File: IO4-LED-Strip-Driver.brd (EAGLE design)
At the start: 109.9 x 100 mm, 21 parts, among them Q1 DMN4468, Q2 DMN4468, Q3 DMN4468, Q7 DMN4468

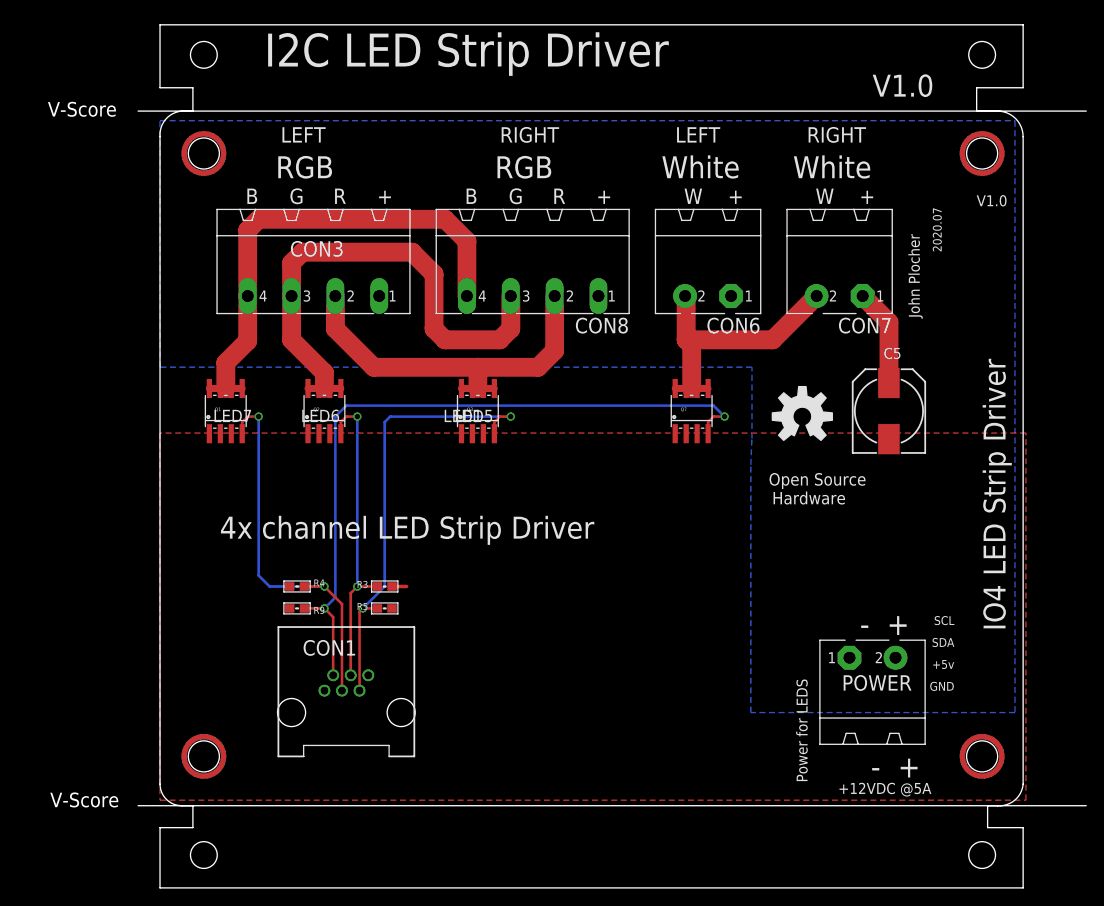
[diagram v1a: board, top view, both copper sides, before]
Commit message: silkscreen changes
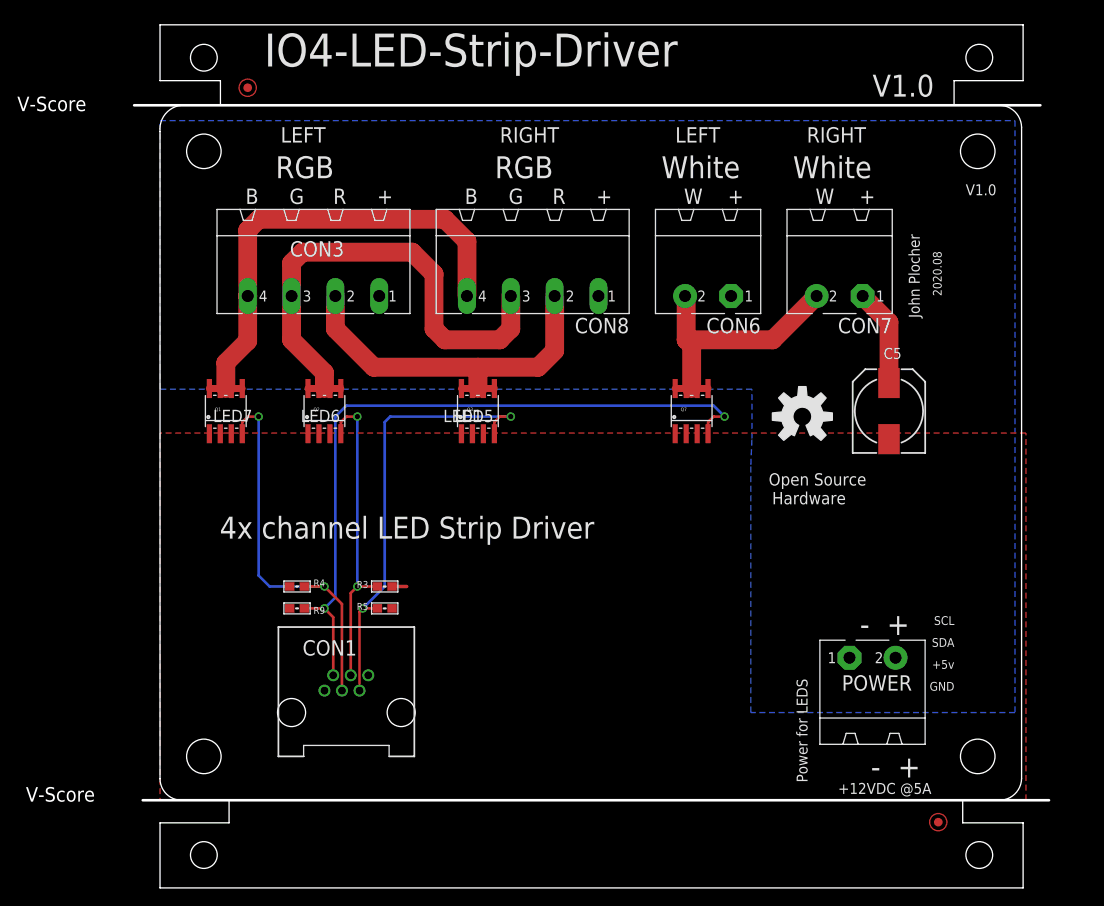
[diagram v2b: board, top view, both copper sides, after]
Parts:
- removed U$1, U$2, U$3, U$4: MOUNTINGHOLE, SPCoast:MOUNTINGHOLE
- added FID1, FID2: FIDUCIAL, SPCoast:FIDUCIAL_1MM
- BOARD1: value BOARD80X100-TEMPLATE -> BOARD80X100; device SPCoast:BOARD-10X8-TEMPLATE -> SPCoast:BOARD-DINRAIL-3.17INX10CM
- C5: value 150uF -> 220uF
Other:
- board size 109.9 x 100 mm -> 106 x 100 mm
- board text added: "2020.08"
- board text added: ">DRAWING_NAME"
- board text removed: "2020.07"
- board text removed: "I2C LED Strip Driver"
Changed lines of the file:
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@@
 <grid distance="50" unitdist="mil" unit="mil" style="dots" multiple="2" display="yes" altdistance="25" altunitdist="mil" altunit="mil"/>
 <layers>
-<layer number="1" name="Top" color="4" fill="1" visible="no" active="yes"/>
-<layer number="16" name="Bottom" color="2" fill="1" visible="no" active="yes"/>
+<layer number="1" name="Top" color="4" fill="1" visible="yes" active="yes"/>
+<layer number="16" name="Bottom" color="2" fill="1" visible="yes" active="yes"/>
 <layer number="17" name="Pads" color="23" fill="1" visible="yes" active="yes"/>
 <layer number="18" name="Vias" color="29" fill="1" visible="yes" active="yes"/>
-<layer number="19" name="Unrouted" color="6" fill="1" visible="no" active="yes"/>
+<layer number="19" name="Unrouted" color="6" fill="1" visible="yes" active="yes"/>
 <layer number="20" name="Dimension" color="15" fill="1" visible="yes" active="yes"/>
 <layer number="21" name="tPlace" color="19" fill="1" visible="yes" active="yes"/>
 <layer number="22" name="bPlace" color="17" fill="1" visible="no" active="yes"/>
-<layer number="23" name="tOrigins" color="30" fill="1" visible="no" active="yes"/>
+<layer number="23" name="tOrigins" color="30" fill="1" visible="yes" active="yes"/>
 <layer number="24" name="bOrigins" color="15" fill="1" visible="no" active="yes"/>
-<layer number="25" name="tNames" color="63" fill="1" visible="no" active="yes"/>
+<layer number="25" name="tNames" color="63" fill="1" visible="yes" active="yes"/>
 <layer number="26" name="bNames" color="34" fill="1" visible="no" active="yes"/>
 <layer number="27" name="tValues" color="56" fill="1" visible="yes" active="yes"/>
@@
 <layer number="42" name="bRestrict" color="3" fill="10" visible="no" active="yes"/>
 <layer number="43" name="vRestrict" color="2" fill="10" visible="no" active="yes"/>
-<layer number="44" name="Drills" color="16" fill="1" visible="no" active="yes"/>
-<layer number="45" name="Holes" color="35" fill="1" visible="no" active="yes"/>
+<layer number="44" name="Drills" color="16" fill="1" visible="yes" active="yes"/>
+<layer number="45" name="Holes" color="35" fill="1" visible="yes" active="yes"/>
 <layer number="46" name="Milling" color="50" fill="1" visible="yes" active="yes"/>
-<layer number="47" name="Measures" color="21" fill="1" visible="no" active="yes"/>
+<layer number="47" name="Measures" color="21" fill="1" visible="yes" active="yes"/>
 <layer number="48" name="Document" color="24" fill="1" visible="yes" active="yes"/>
-<layer number="49" name="Reference" color="48" fill="1" visible="no" active="yes"/>
+<layer number="49" name="Reference" color="48" fill="1" visible="yes" active="yes"/>
 <layer number="50" name="dxf" color="7" fill="1" visible="no" active="yes"/>
 <layer number="51" name="tDocu" color="24" fill="1" visible="yes" active="yes"/>
@@
 <board>
 <plain>
-<text x="12.065" y="95.17" size="3.81" layer="21" font="vector" ratio="13" distance="49" rot="SR0">I2C LED Strip Driver</text>
-<text x="94.615" y="78.98" size="1.27" layer="21" font="vector" ratio="10">V1.0</text>
+<text x="12.065" y="95.17" size="3.81" layer="21" font="vector" ratio="13" distance="49" rot="SR0">&gt;DRAWING_NAME</text>
+<text x="93.345" y="80.25" size="1.27" layer="21" font="vector" ratio="10">V1.0</text>
 <text x="9.033" y="13.1318" size="1.778" layer="52" rot="MR180">Made in the PCR, Coast Division, NMRA</text>
 <text x="91.0418" y="11.7152" size="1.4224" layer="52" font="vector" ratio="15" rot="MR0">www. SP Coast .com</text>
@@
 <wire x1="3.953" y1="27.305" x2="11.573" y2="66.802" width="3.81" layer="52"/>
 <text x="89.37625" y="12.16025" size="1.27" layer="21" font="vector" rot="R180">+12VDC @5A</text>
-<text x="97.959971875" y="29.76735625" size="2.54" layer="21" font="vector" ratio="15" rot="SR90">IO4 LED Strip Driver</text>
+<text x="93.810028125" y="78.18264375" size="2.54" layer="21" font="vector" ratio="15" rot="R270">&gt;DRAWING_NAME</text>
 <wire x1="0" y1="60.96" x2="100.33" y2="46.99" width="2.1844" layer="52"/>
 <wire x1="0" y1="35.56" x2="100.33" y2="21.59" width="2.1844" layer="52"/>
@@
 <text x="92.04200625" y="26.402490625" size="1.016" layer="21" font="vector" ratio="10" rot="R180">+5v</text>
 <text x="92.04200625" y="23.862490625" size="1.016" layer="21" font="vector" ratio="10" rot="R180">GND</text>
-<text x="90.565" y="73.66" size="1.016" layer="21" font="vector" ratio="10" rot="R90">2020.07</text>
+<text x="90.565" y="68.58" size="1.016" layer="21" font="vector" ratio="10" rot="R90">2020.08</text>
 <text x="88.025" y="66.04" size="1.27" layer="21" font="vector" ratio="10" rot="R90">John Plocher</text>
 <text x="75.02525" y="12.22375" size="1.27" layer="21" font="vector" rot="R90">Power for LEDS</text>
@@
 </autorouter>
 <elements>
-<element name="BOARD1" library="SPCoast" package="BOARD-10X8-TEMPLATE" value="BOARD80X100-TEMPLATE" x="0" y="0"/>
+<element name="BOARD1" library="SPCoast" package="BOARD-DINRAIL-3.17INX10CM" value="BOARD80X100" x="0" y="0"/>
 <element name="OSHW1" library="SparkFun" package="OSHW-LOGO-L" value="OSHW-LOGOL" x="74.422" y="54.61"/>
-<element name="C5" library="SPCoast" package="0810-CAP" value="150uF" x="84.455" y="55.245" smashed="yes" rot="R90">
+<element name="C5" library="SPCoast" package="0810-CAP" value="220uF" x="84.455" y="55.245" smashed="yes" rot="R90">
 <attribute name="NAME" x="85.925" y="62.565" size="1.27" layer="25" rot="R180"/>
 <attribute name="VALUE" x="87.63" y="55.88" size="1.27" layer="27" font="vector" rot="R180"/>
@@
 <attribute name="VALUE" x="77.47" y="21.59" size="1.778" layer="27" ratio="10"/>
 </element>
-<element name="U$1" library="SPCoast" package="MOUNTINGHOLE" value="MOUNTINGHOLE" x="5.08" y="15.24"/>
-<element name="U$2" library="SPCoast" package="MOUNTINGHOLE" value="MOUNTINGHOLE" x="95.25" y="15.24"/>
-<element name="U$4" library="SPCoast" package="MOUNTINGHOLE" value="MOUNTINGHOLE" x="95.25" y="85.09"/>
-<element name="U$3" library="SPCoast" package="MOUNTINGHOLE" value="MOUNTINGHOLE" x="5.08" y="85.09"/>
 <element name="R5" library="SPCoast" package="0603-RES" value="10k" x="26.035" y="32.385" smashed="yes" rot="R180">
 <attribute name="NAME" x="24.13" y="33.02" size="0.8128" layer="25" font="vector" rot="R180"/>
@@
 <element name="CON7" library="SPCoast" package="MSTBA2" value="" x="78.74" y="73.66" rot="R180"/>
 <element name="CON8" library="SPCoast" package="MSTBA4" value="" x="43.18" y="73.66" rot="R180"/>
+<element name="FID1" library="SPCoast" package="FIDUCIAL_1MM" value="FIDUCIAL" x="10.16" y="92.71"/>
+<element name="FID2" library="SPCoast" package="FIDUCIAL_1MM" value="FIDUCIAL" x="90.17" y="7.62"/>
 </elements>
 <signals>
@@
 <vertex x="68.453" y="49.022"/>
 <vertex x="68.58" y="52.07"/>
-<vertex x="68.58" y="60.325"/>
-<vertex x="0" y="60.325"/>
+<vertex x="68.58" y="57.785"/>
+<vertex x="0" y="57.785"/>
 <vertex x="0" y="88.9"/>
 <vertex x="99.06" y="88.9"/>
